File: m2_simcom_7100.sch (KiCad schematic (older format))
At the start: 30 parts, among them J1 M.2_Key_B, Q1 NC, U1 SIM7100

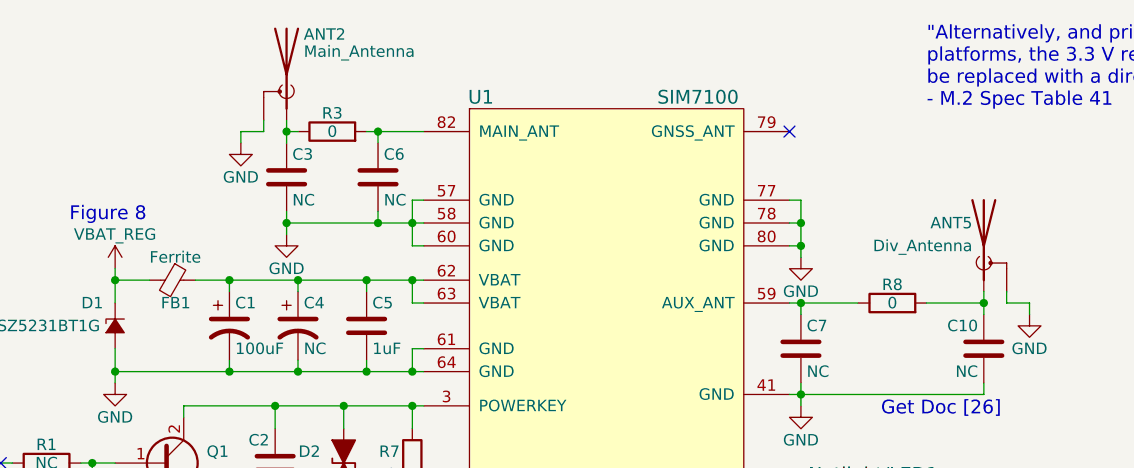
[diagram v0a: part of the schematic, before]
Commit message: Use the RT9059 LDO in the layout instead of the old MIC29302 one
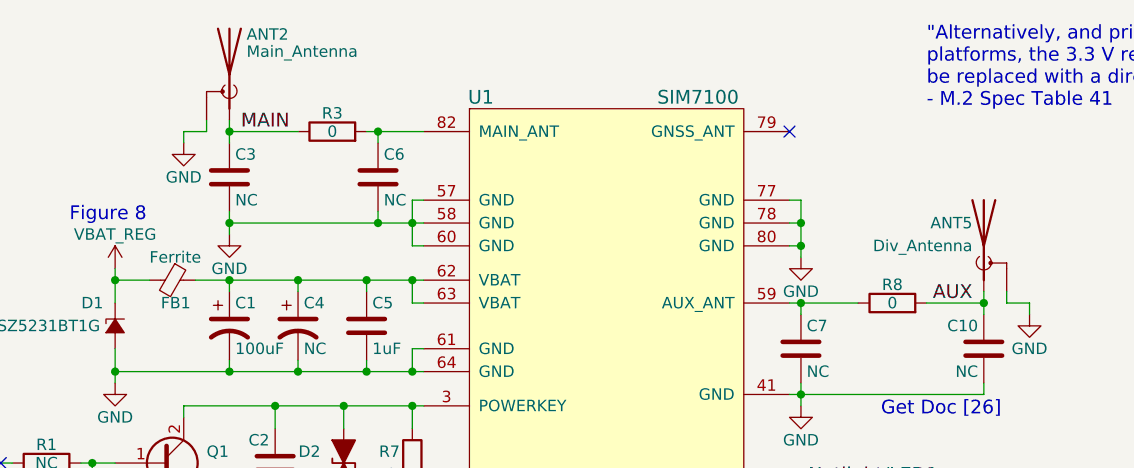
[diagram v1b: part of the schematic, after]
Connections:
- net MAIN: now reaches ANT2.1 (A), C3.1, R3.1
- net AUX: now reaches ANT5.1 (A), C10.1, R8.2
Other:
- moved on the sheet: ANT2, C3
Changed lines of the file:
@@
 L Antenna_Shield ANT2
 U 1 1 5AB020C9
-P 3600 800
-F 0 "ANT2" H 3525 975 50  0000 R CNN
-F 1 "Main_Antenna" H 3525 900 50  0000 R CNN
-F 2 "m2_simcom_7100:MHF4_20449-001E" H 3600 900 50  0001 C CNN
-F 3 "https://www.mouser.com/ds/2/398/RECE.20449.001E.01-27117.pdf" H 3600 900 50  0001 C CNN
-	1    3600 800
+P 3350 800
+F 0 "ANT2" H 3275 975 50  0000 R CNN
+F 1 "Main_Antenna" H 3275 900 50  0000 R CNN
+F 2 "m2_simcom_7100:MHF4_20449-001E" H 3350 900 50  0001 C CNN
+F 3 "https://www.mouser.com/ds/2/398/RECE.20449.001E.01-27117.pdf" H 3350 900 50  0001 C CNN
+	1    3350 800
 	-1   0    0    -1
 $EndComp
@@
 L GND #PWR04
 U 1 1 5AB023EB
-P 3400 1100
-F 0 "#PWR04" H 3400 850 50  0001 C CNN
-F 1 "GND" H 3400 950 50  0000 C CNN
-F 2 "" H 3400 1100 50  0001 C CNN
-F 3 "" H 3400 1100 50  0001 C CNN
-	1    3400 1100
+P 3150 1100
+F 0 "#PWR04" H 3150 850 50  0001 C CNN
+F 1 "GND" H 3150 950 50  0000 C CNN
+F 2 "" H 3150 1100 50  0001 C CNN
+F 3 "" H 3150 1100 50  0001 C CNN
+	1    3150 1100
 	1    0    0    -1
 $EndComp
@@
 L C C3
 U 1 1 5AB02470
-P 3600 1250
-F 0 "C3" H 3625 1350 50  0000 L CNN
-F 1 "NC" H 3625 1150 50  0000 L CNN
-F 2 "Capacitors_SMD:C_0603" H 3638 1100 50  0001 C CNN
-F 3 "" H 3600 1250 50  0001 C CNN
-	1    3600 1250
+P 3350 1250
+F 0 "C3" H 3375 1350 50  0000 L CNN
+F 1 "NC" H 3375 1150 50  0000 L CNN
+F 2 "Capacitors_SMD:C_0603" H 3388 1100 50  0001 C CNN
+F 3 "" H 3350 1250 50  0001 C CNN
+	1    3350 1250
 	1    0    0    -1
 $EndComp
@@
 L GND #PWR013
 U 1 1 5AC373E0
-P 3600 1500
-F 0 "#PWR013" H 3600 1250 50  0001 C CNN
-F 1 "GND" H 3600 1350 50  0000 C CNN
-F 2 "" H 3600 1500 50  0001 C CNN
-F 3 "" H 3600 1500 50  0001 C CNN
-	1    3600 1500
+P 3350 1500
+F 0 "#PWR013" H 3350 1250 50  0001 C CNN
+F 1 "GND" H 3350 1350 50  0000 C CNN
+F 2 "" H 3350 1500 50  0001 C CNN
+F 3 "" H 3350 1500 50  0001 C CNN
+	1    3350 1500
 	1    0    0    -1
 $EndComp
@@
 	3950 1050 4200 1050
 Wire Wire Line
-	3600 1000 3600 1100
-Wire Wire Line
-	3600 1450 4200 1450
-Wire Wire Line
-	3600 1400 3600 1500
-Connection ~ 3600 1050
+	3350 1000 3350 1100
+Wire Wire Line
+	3350 1450 4200 1450
+Wire Wire Line
+	3350 1400 3350 1500
+Connection ~ 3350 1050
 Wire Wire Line
 	4200 1350 4150 1350
@@
 Connection ~ 4000 1050
 Wire Wire Line
-	3400 1100 3400 1050
-Wire Wire Line
-	3400 1050 3500 1050
-Wire Wire Line
-	3500 1050 3500 1000
-Wire Wire Line
-	3650 1050 3600 1050
+	3150 1100 3150 1050
+Wire Wire Line
+	3150 1050 3250 1050
+Wire Wire Line
+	3250 1050 3250 1000
+Wire Wire Line
+	3650 1050 3350 1050
 Wire Wire Line
 	2850 1650 2850 1800
@@
 	4200 1800 4150 1800
 Wire Wire Line
-	4150 1800 4150 1700
+	4150 1700 4150 1800
 Connection ~ 4150 1700
 Wire Wire Line
@@
 Wire Wire Line
 	8700 5900 7750 5900
-Connection ~ 3600 1450
+Connection ~ 3350 1450
 Wire Wire Line
 	9400 5750 9400 5700
@@
 	0    1    1    0
 $EndComp
+Text Label 3400 1050 0    60   ~ 0
+MAIN
+Text Label 6600 1800 2    60   ~ 0
+AUX
 $EndSCHEMATC

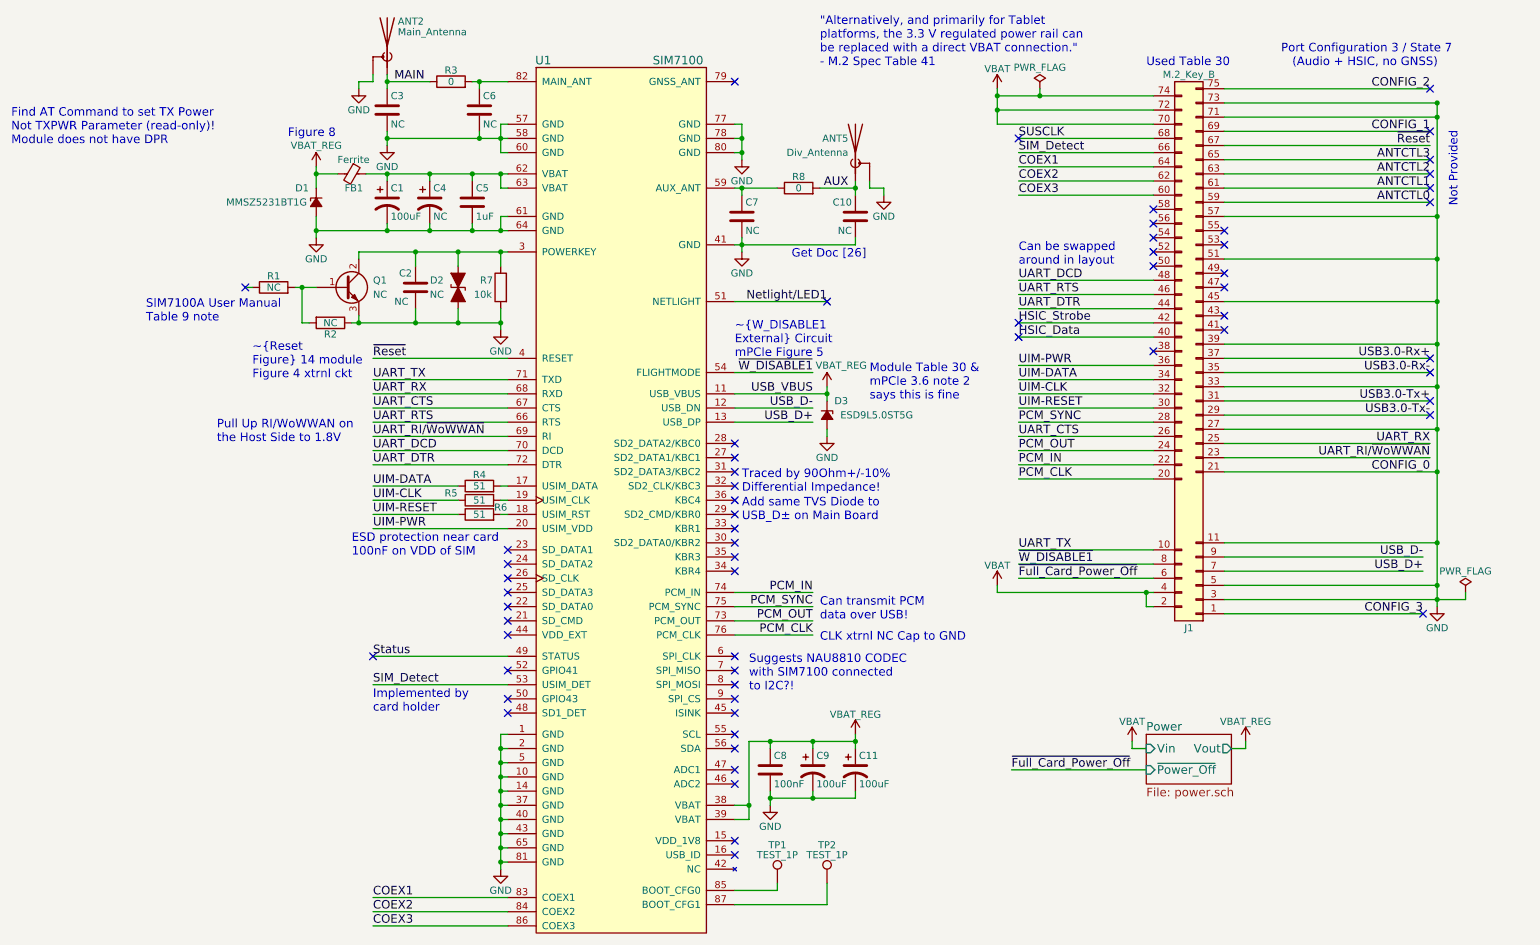
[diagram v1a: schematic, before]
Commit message: Add 74AUP1G04 schmitt-triggered inverter to SIM_DET based on the fact that most WWAN M.2 modules expect this to be an active HIGH input
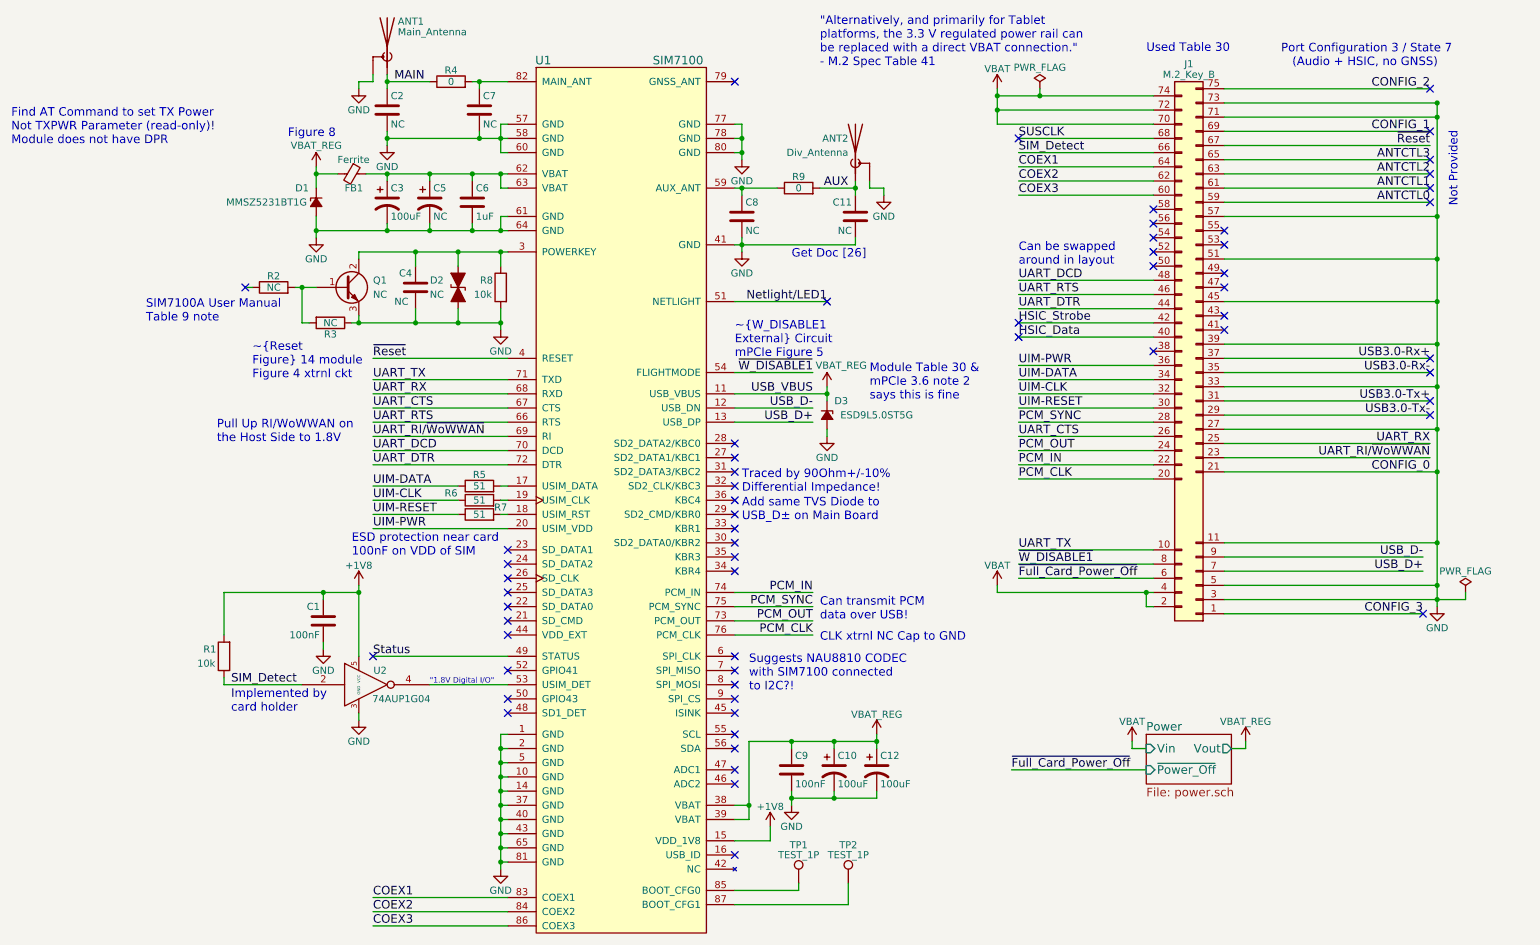
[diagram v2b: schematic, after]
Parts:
- added C1: 100nF, symbol C
- added R1: 10k, symbol R
- added U2: 74AUP1G04, symbol 74AHC1G14
- renumbered ANT2 to ANT1, ANT5 to ANT2, C9 to C10, C10 to C11, C11 to C12, C3 to C2, C1 to C3, C2 to C4, C4 to C5, C5 to C6, C6 to C7, C7 to C8, C8 to C9, R1 to R2, R2 to R3, R3 to R4, R4 to R5, R5 to R6, R6 to R7, R7 to R8, R8 to R9
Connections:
- net GND: now also C1.2, U2.3 (GND)
- net SIM_Detect: now also R1.1, U2.2; no longer U1.53 (USIM_DET)
- net +1V8: now reaches U1.15 (VDD_1V8)
- net +1V8: now also C1.1, R1.2, U2.5 (VCC)
- new net: U1.53 (USIM_DET), U2.4
- no-connect marks 61 -> 60
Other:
- note added: ""1.8V Digital I/O""
- moved on the sheet: C10, C12, C9, TP1, TP2

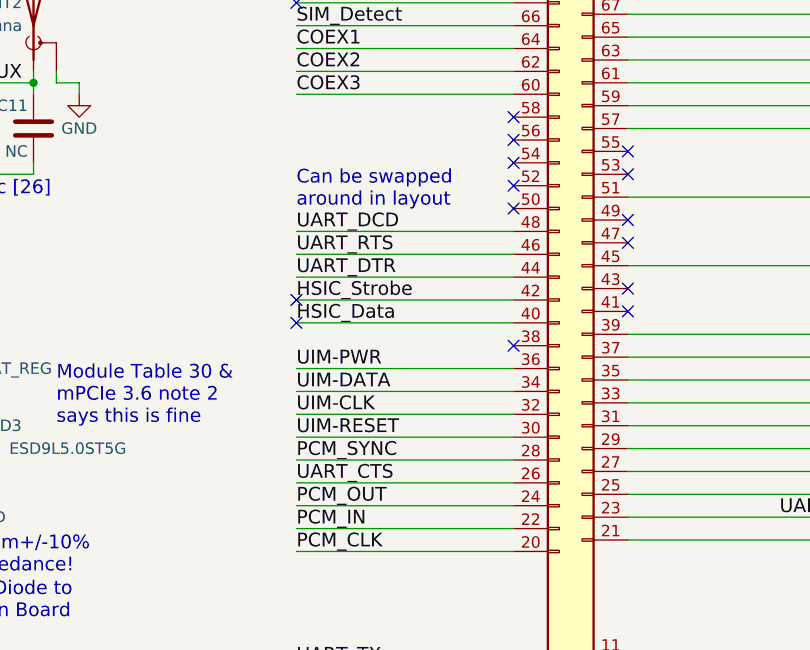
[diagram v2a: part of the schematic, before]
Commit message: Make UART interface null modem instead of full modem
Full modem is unnecessary since the modem can be woken via USB. There's no dedicated DTR, DSR, or DCD lines on the i.MX8M. Generally simpler to implement standard UART (Null Modem).
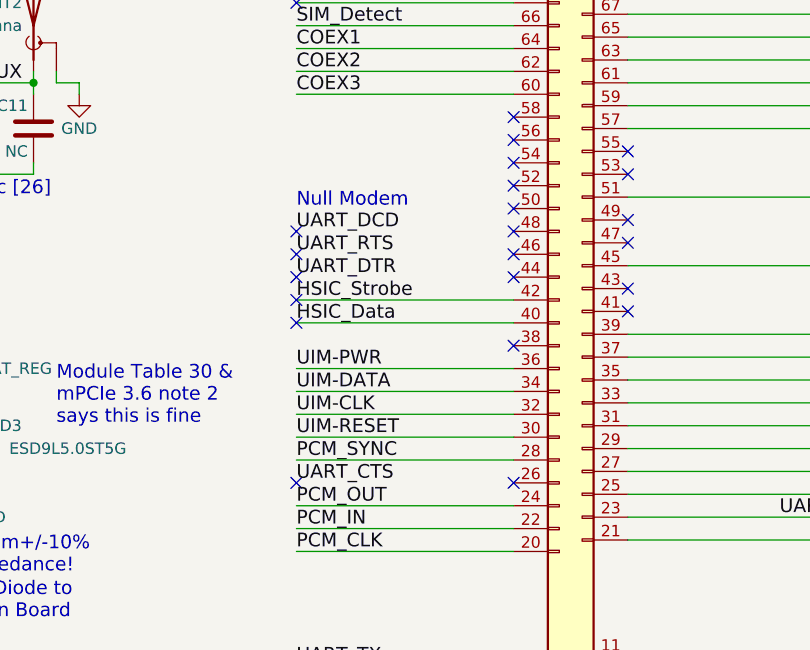
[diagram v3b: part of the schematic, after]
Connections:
- net UART_CTS: no longer J1.26 (Pin_26)
- net UART_DCD: no longer J1.48 (Pin_48)
- net UART_DTR: no longer J1.44 (Pin_44)
- net UART_RTS: no longer J1.46 (Pin_46)
- no-connect marks 60 -> 68
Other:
- note added: "Null Modem"
- note removed: "Can be swapped\naround in layout"
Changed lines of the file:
@@
 Text Label 7800 3550 0    60   ~ 0
 UART_CTS
-Text Label 7800 2550 0    60   ~ 0
-UART_RTS
-Text Label 7800 2450 0    60   ~ 0
-UART_DCD
-Text Label 7800 2650 0    60   ~ 0
-UART_DTR
 NoConn ~ 10700 1100
 NoConn ~ 10700 1400
@@
 UART_RI/~WoWWAN
 Text Notes 7800 2350 0    60   ~ 0
-Can be swapped\naround in layout
+Null Modem
 Text Notes 2150 3600 0    60   ~ 0
 Pull Up RI/WoWWAN on\nthe Host Side to 1.8V
@@
 	8750 1850 7800 1850
 Wire Wire Line
-	8750 2450 7800 2450
-Wire Wire Line
-	8750 2550 7800 2550
-Wire Wire Line
-	8750 2650 7800 2650
-Wire Wire Line
 	8750 2750 7800 2750
 Wire Wire Line
@@
 Wire Wire Line
 	8750 3450 7800 3450
-Wire Wire Line
-	8750 3550 7800 3550
 Wire Wire Line
 	8750 3650 7800 3650
@@
 Text Notes 3650 5300 0    39   ~ 0
 "1.8V Digital I/O"
+Text Label 7800 2450 0    60   ~ 0
+UART_DCD
+Text Label 7800 2550 0    60   ~ 0
+UART_RTS
+Text Label 7800 2650 0    60   ~ 0
+UART_DTR
+NoConn ~ 7800 2550
+NoConn ~ 7800 2650
+NoConn ~ 8750 2450
+NoConn ~ 8750 2550
+NoConn ~ 8750 2650
+NoConn ~ 7800 2450
+NoConn ~ 7800 3550
+NoConn ~ 8750 3550
 $EndSCHEMATC
